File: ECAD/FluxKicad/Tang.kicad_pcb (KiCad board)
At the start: 2 copper layers, 39 x 60 mm, 26 parts, among them SW1 SW_SPST, SW2 SW_SPST, SW3 RotaryEncoder, U1 SeeeduinoXIAO, U2 DRV5056A3QDBZx Lekker, U3 DRV5056A3QDBZx Lekker

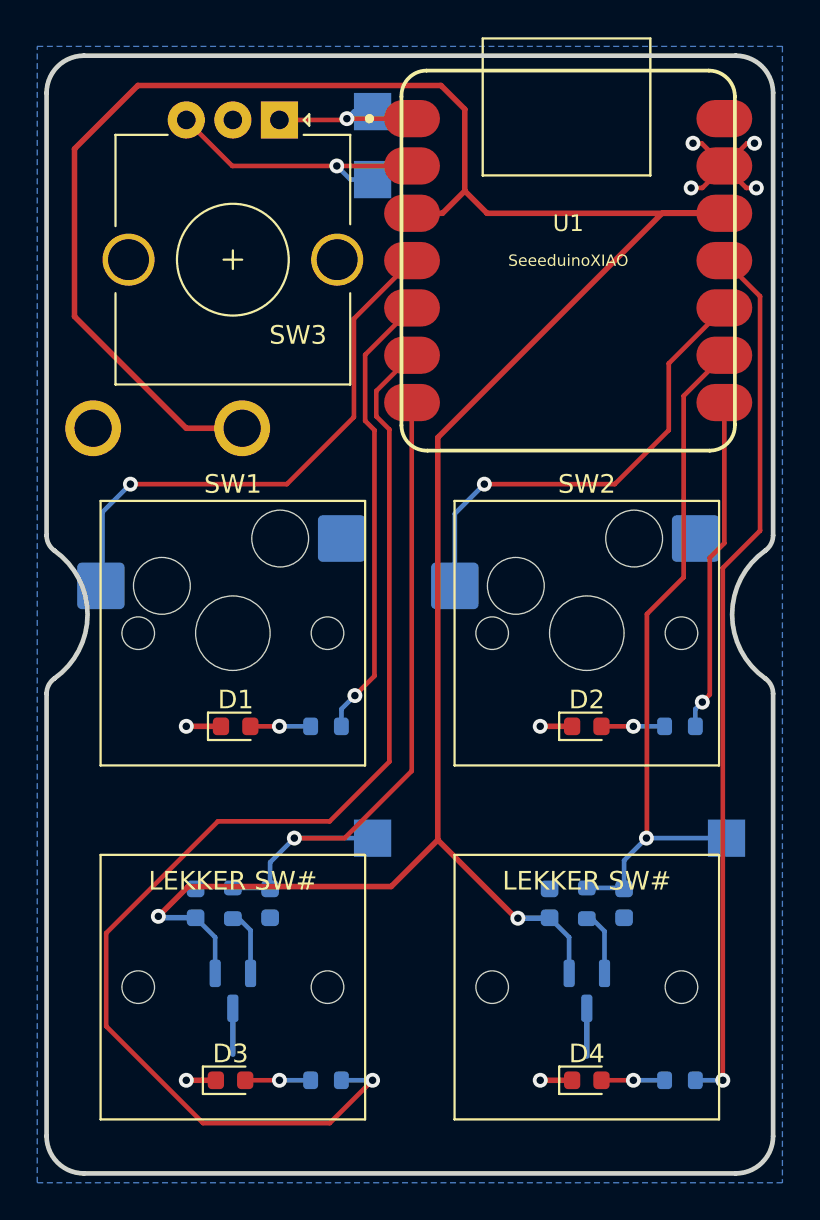
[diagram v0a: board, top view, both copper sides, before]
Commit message: added encoder, added voltage buffer
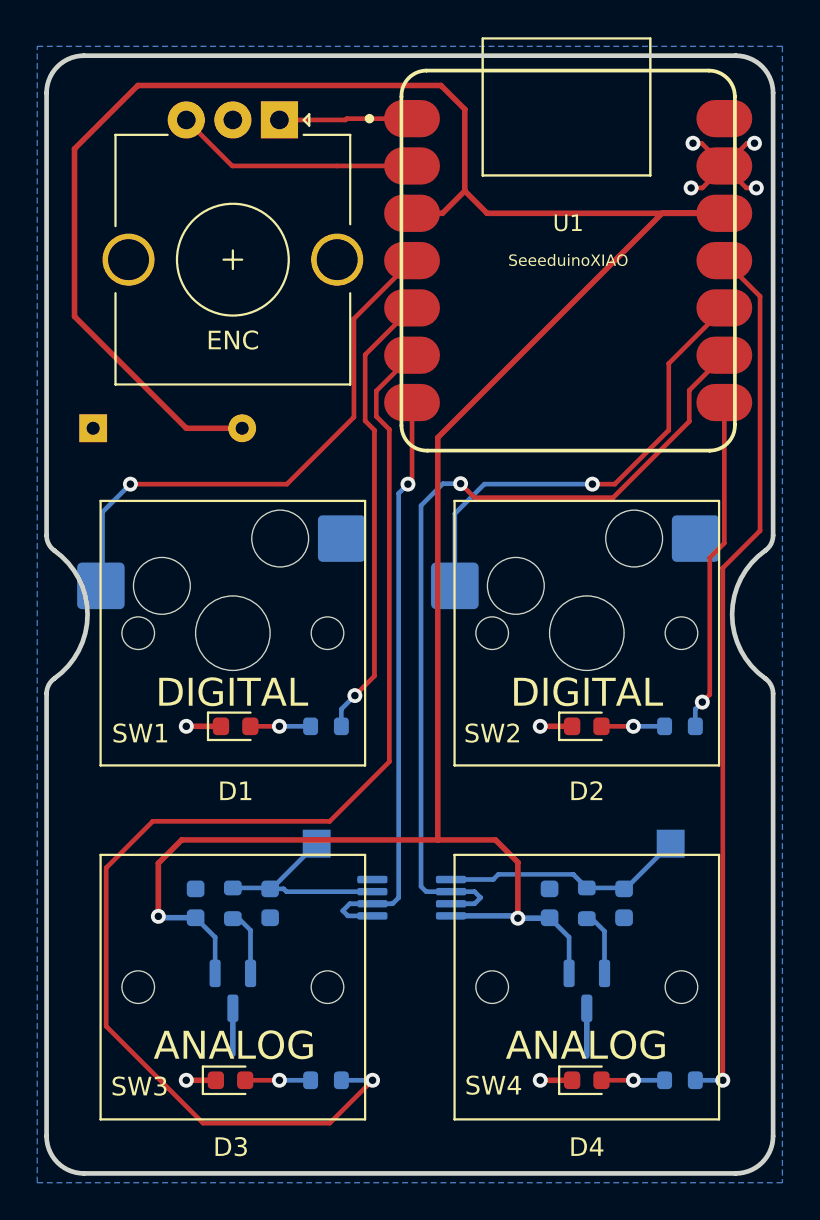
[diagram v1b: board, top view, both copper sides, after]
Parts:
- removed ENCA1, ENCB1: TestPoint, TestPoint:TestPoint_Pad_2.0x2.0mm
- added U4: LMV358DMR2G, Package_SO:MSOP-8_3x3mm_P0.65mm, B.Cu at (120.1, 110.2)
- 3V3: footprint TestPoint:TestPoint_Plated_Hole_D2.0mm -> TestPoint:TestPoint_THTPad_D1.5mm_Drill0.7mm
- GND1: footprint TestPoint:TestPoint_Plated_Hole_D2.0mm -> TestPoint:TestPoint_THTPad_1.5x1.5mm_Drill0.7mm
- R1, R2, R3, R4: value 10 -> 20
- TP_SW3, TP_SW4: footprint TestPoint:TestPoint_Pad_2.0x2.0mm -> TestPoint:TestPoint_Pad_1.5x1.5mm
- moved TP_SW3 3.01 mm to (115.0, 107.3)
- moved TP_SW4 3.01 mm to (134.0, 107.3)
- renumbered SW3 to ENC
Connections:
- U1 pad 7: SW3 -> SW3_BUF
- U1 pad 9: SW4 -> SW4_BUF
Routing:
- net SW4_BUF: track 0.00 -> 46.8 mm, vias 0 -> 1
- net SW3_BUF: track 0.00 -> 31.9 mm, vias 0 -> 1
- net SW3: track 37.1 -> 11.1 mm, vias 1 -> 0
- net SW4: track 37.2 -> 13.2 mm, vias 1 -> 0
- net +3V3: track 140.4 -> 147.5 mm
- net ENCB: track 15.6 -> 13.4 mm, vias 1 -> 0
- net LED3: track 65.9 -> 68.0 mm
- net ENCA: track 8.92 -> 7.38 mm, vias 1 -> 0
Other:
- board text added: "ANALOG"
- board text added: "DIGITAL"

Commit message: added lighting, update cad
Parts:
- removed U4: LMV358DMR2G, Package_SO:MSOP-8_3x3mm_P0.65mm
- 3V3: footprint TestPoint:TestPoint_THTPad_D1.5mm_Drill0.7mm -> TestPoint:TestPoint_Pad_1.0x1.0mm
- GND1: footprint TestPoint:TestPoint_THTPad_1.5x1.5mm_Drill0.7mm -> TestPoint:TestPoint_Pad_1.0x1.0mm
- SW3: renamed from ENC; value RotaryEncoder -> PEC12R-4017F-N0024
- TP_SW3, TP_SW4: footprint TestPoint:TestPoint_Pad_1.5x1.5mm -> TestPoint:TestPoint_Pad_1.0x1.0mm
- moved GND1 20.8 mm to (123.1, 79.5)
- moved 3V3 15.7 mm to (123.1, 75.0)
- moved TP_SW3 2.55 mm to (112.5, 107.8)
- moved TP_SW4 2.55 mm to (131.5, 107.8)
- moved D3 0.12 mm to (110.5, 120.0)
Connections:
- U1 pad 7: SW3_BUF -> SW3
- U1 pad 9: SW4_BUF -> SW4
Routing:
- net +3V3: track 147.5 -> 94.8 mm, vias 2 -> 3
- net SW4_BUF: track 46.8 -> 0.00 mm, vias 1 -> 0
- net SW4: track 13.2 -> 51.3 mm, vias 0 -> 1
- net SW3_BUF: track 31.9 -> 0.00 mm, vias 1 -> 0
- net SW3: track 11.1 -> 36.4 mm, vias 0 -> 1
- net LED3: track 68.0 -> 77.0 mm
- net SW1: track 29.4 -> 30.9 mm
- net SW2: track 25.0 -> 26.4 mm

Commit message: add more images, update schematic and pcb, update fw
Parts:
- added TP_SW1: TestPoint, TestPoint:TestPoint_Pad_1.0x1.0mm, B.Cu at (104.0, 100.0)
- added TP_SW2: TestPoint, TestPoint:TestPoint_Pad_1.0x1.0mm, B.Cu at (123.0, 100.0)
- moved GND1 8.74 mm to (131.6, 77.5)
- moved 3V3 8.63 mm to (131.6, 73.5)
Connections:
- U1 pad 3: +3V3 -> SW1
- U1 pad 4: SW1 -> LED1
- U1 pad 5: LED1 -> unconnected-(U1-Pad5)
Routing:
- net +3V3: track 94.8 -> 79.1 mm
- net SW1: track 30.9 -> 40.2 mm
- net SW2: track 26.4 -> 33.6 mm
- net LED1: track 24.9 -> 31.1 mm, vias 1 -> 3
